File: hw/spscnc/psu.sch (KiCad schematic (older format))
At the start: 35 parts

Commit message: began routing of the i2so part
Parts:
- removed H17, H18, H21, H22, H23, H26, H28, H31: MountingHole_Pad, MountingHole:MountingHole_2.2mm_M2_Pad_Via, symbol Mechanical:MountingHole_Pad

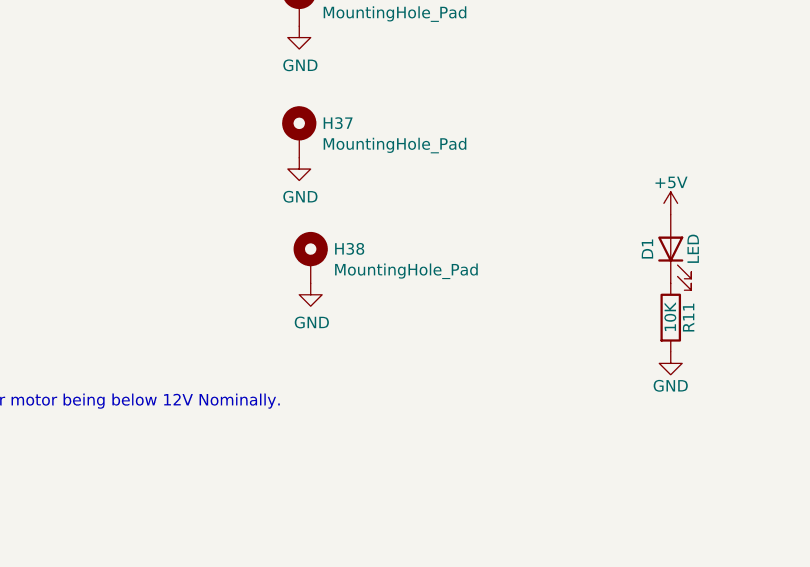
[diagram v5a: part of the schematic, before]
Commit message: Revision 1.1.0 With only critical corrections. Pending some work on the relays as that part could be remade from scratch for flexibility.
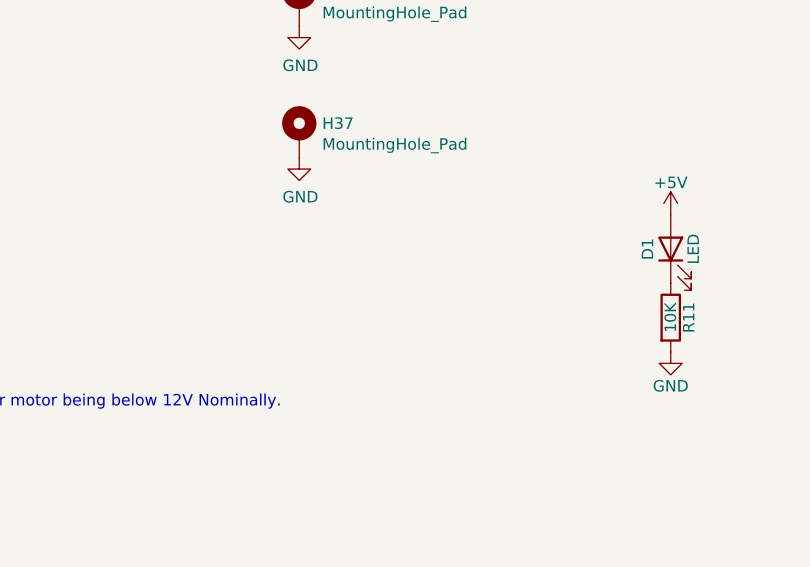
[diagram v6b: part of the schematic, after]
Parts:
- removed H38: MountingHole_Pad, MountingHole:MountingHole_2.2mm_M2_Pad_Via, symbol Mechanical:MountingHole_Pad
- H1, H11, H12, H13, H14, H15, H16, H19, H2, H20, H24, H25, H27, H29, H30, H32, H33, H34, H35, H36, H37: footprint MountingHole:MountingHole_2.2mm_M2_Pad_Via -> MountingHole:MountingHole_3.2mm_M3_Pad_Via
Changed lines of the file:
@@
 Sheet 2 17
 Title "Trinamic FluidNC CNC Controller"
-Date "2022-02-12"
-Rev "1.0.1"
+Date "2022-04-29"
+Rev "1.1.0"
 Comp ""
 Comment1 ""
@@
 F 0 "H1" H 6000 1474 50  0000 L CNN
 F 1 "MountingHole_Pad" H 6000 1383 50  0000 L CNN
-F 2 "MountingHole:MountingHole_2.2mm_M2_Pad_Via" H 5900 1425 50  0001 C CNN
+F 2 "MountingHole:MountingHole_3.2mm_M3_Pad_Via" H 5900 1425 50  0001 C CNN
 F 3 "~" H 5900 1425 50  0001 C CNN
 F 4 "DNP003" H 5900 1425 50  0001 C CNN "jlcpcb"
@@
 F 0 "H13" H 7250 1474 50  0000 L CNN
 F 1 "MountingHole_Pad" H 7250 1383 50  0000 L CNN
-F 2 "MountingHole:MountingHole_2.2mm_M2_Pad_Via" H 7150 1425 50  0001 C CNN
+F 2 "MountingHole:MountingHole_3.2mm_M3_Pad_Via" H 7150 1425 50  0001 C CNN
 F 3 "~" H 7150 1425 50  0001 C CNN
 F 4 "DNP003" H 7150 1425 50  0001 C CNN "jlcpcb"
@@
 F 0 "H12" H 6000 1999 50  0000 L CNN
 F 1 "MountingHole_Pad" H 6000 1908 50  0000 L CNN
-F 2 "MountingHole:MountingHole_2.2mm_M2_Pad_Via" H 5900 1950 50  0001 C CNN
+F 2 "MountingHole:MountingHole_3.2mm_M3_Pad_Via" H 5900 1950 50  0001 C CNN
 F 3 "~" H 5900 1950 50  0001 C CNN
 F 4 "DNP003" H 5900 1950 50  0001 C CNN "jlcpcb"
@@
 F 0 "H14" H 7250 2024 50  0000 L CNN
 F 1 "MountingHole_Pad" H 7250 1933 50  0000 L CNN
-F 2 "MountingHole:MountingHole_2.2mm_M2_Pad_Via" H 7150 1975 50  0001 C CNN
+F 2 "MountingHole:MountingHole_3.2mm_M3_Pad_Via" H 7150 1975 50  0001 C CNN
 F 3 "~" H 7150 1975 50  0001 C CNN
 F 4 "DNP003" H 7150 1975 50  0001 C CNN "jlcpcb"
@@
 F 0 "H2" H 5975 2574 50  0000 L CNN
 F 1 "MountingHole_Pad" H 5975 2483 50  0000 L CNN
-F 2 "MountingHole:MountingHole_2.2mm_M2_Pad_Via" H 5875 2525 50  0001 C CNN
+F 2 "MountingHole:MountingHole_3.2mm_M3_Pad_Via" H 5875 2525 50  0001 C CNN
 F 3 "~" H 5875 2525 50  0001 C CNN
 F 4 "DNP003" H 5875 2525 50  0001 C CNN "jlcpcb"
@@
 F 0 "H15" H 7275 2574 50  0000 L CNN
 F 1 "MountingHole_Pad" H 7275 2483 50  0000 L CNN
-F 2 "MountingHole:MountingHole_2.2mm_M2_Pad_Via" H 7175 2525 50  0001 C CNN
+F 2 "MountingHole:MountingHole_3.2mm_M3_Pad_Via" H 7175 2525 50  0001 C CNN
 F 3 "~" H 7175 2525 50  0001 C CNN
 F 4 "DNP003" H 7175 2525 50  0001 C CNN "jlcpcb"
@@
 F 0 "H19" H 8325 2599 50  0000 L CNN
 F 1 "MountingHole_Pad" H 8325 2508 50  0000 L CNN
-F 2 "MountingHole:MountingHole_2.2mm_M2_Pad_Via" H 8225 2550 50  0001 C CNN
+F 2 "MountingHole:MountingHole_3.2mm_M3_Pad_Via" H 8225 2550 50  0001 C CNN
 F 3 "~" H 8225 2550 50  0001 C CNN
 F 4 "DNP003" H 8225 2550 50  0001 C CNN "jlcpcb"
@@
 F 0 "H11" H 5975 3174 50  0000 L CNN
 F 1 "MountingHole_Pad" H 5975 3083 50  0000 L CNN
-F 2 "MountingHole:MountingHole_2.2mm_M2_Pad_Via" H 5875 3125 50  0001 C CNN
+F 2 "MountingHole:MountingHole_3.2mm_M3_Pad_Via" H 5875 3125 50  0001 C CNN
 F 3 "~" H 5875 3125 50  0001 C CNN
 F 4 "DNP003" H 5875 3125 50  0001 C CNN "jlcpcb"
@@
 F 0 "H16" H 7300 3149 50  0000 L CNN
 F 1 "MountingHole_Pad" H 7300 3058 50  0000 L CNN
-F 2 "MountingHole:MountingHole_2.2mm_M2_Pad_Via" H 7200 3100 50  0001 C CNN
+F 2 "MountingHole:MountingHole_3.2mm_M3_Pad_Via" H 7200 3100 50  0001 C CNN
 F 3 "~" H 7200 3100 50  0001 C CNN
 F 4 "DNP003" H 7200 3100 50  0001 C CNN "jlcpcb"
@@
 F 0 "H20" H 8375 3149 50  0000 L CNN
 F 1 "MountingHole_Pad" H 8375 3058 50  0000 L CNN
-F 2 "MountingHole:MountingHole_2.2mm_M2_Pad_Via" H 8275 3100 50  0001 C CNN
+F 2 "MountingHole:MountingHole_3.2mm_M3_Pad_Via" H 8275 3100 50  0001 C CNN
 F 3 "~" H 8275 3100 50  0001 C CNN
 F 4 "DNP003" H 8275 3100 50  0001 C CNN "jlcpcb"
@@
 F 0 "H24" H 9475 3149 50  0000 L CNN
 F 1 "MountingHole_Pad" H 9475 3058 50  0000 L CNN
-F 2 "MountingHole:MountingHole_2.2mm_M2_Pad_Via" H 9375 3100 50  0001 C CNN
+F 2 "MountingHole:MountingHole_3.2mm_M3_Pad_Via" H 9375 3100 50  0001 C CNN
 F 3 "~" H 9375 3100 50  0001 C CNN
 F 4 "DNP003" H 9375 3100 50  0001 C CNN "jlcpcb"
@@
 F 0 "H25" H 10375 1474 50  0000 L CNN
 F 1 "MountingHole_Pad" H 10375 1383 50  0000 L CNN
-F 2 "MountingHole:MountingHole_2.2mm_M2_Pad_Via" H 10275 1425 50  0001 C CNN
+F 2 "MountingHole:MountingHole_3.2mm_M3_Pad_Via" H 10275 1425 50  0001 C CNN
 F 3 "~" H 10275 1425 50  0001 C CNN
 F 4 "DNP003" H 10275 1425 50  0001 C CNN "jlcpcb"
@@
 F 0 "H27" H 10375 2599 50  0000 L CNN
 F 1 "MountingHole_Pad" H 10375 2508 50  0000 L CNN
-F 2 "MountingHole:MountingHole_2.2mm_M2_Pad_Via" H 10275 2550 50  0001 C CNN
+F 2 "MountingHole:MountingHole_3.2mm_M3_Pad_Via" H 10275 2550 50  0001 C CNN
 F 3 "~" H 10275 2550 50  0001 C CNN
 F 4 "DNP003" H 10275 2550 50  0001 C CNN "jlcpcb"
@@
 F 0 "H29" H 10275 3799 50  0000 L CNN
 F 1 "MountingHole_Pad" H 10275 3708 50  0000 L CNN
-F 2 "MountingHole:MountingHole_2.2mm_M2_Pad_Via" H 10175 3750 50  0001 C CNN
+F 2 "MountingHole:MountingHole_3.2mm_M3_Pad_Via" H 10175 3750 50  0001 C CNN
 F 3 "~" H 10175 3750 50  0001 C CNN
 F 4 "DNP003" H 10175 3750 50  0001 C CNN "jlcpcb"
@@
 F 0 "H30" H 10275 4349 50  0000 L CNN
 F 1 "MountingHole_Pad" H 10275 4258 50  0000 L CNN
-F 2 "MountingHole:MountingHole_2.2mm_M2_Pad_Via" H 10175 4300 50  0001 C CNN
+F 2 "MountingHole:MountingHole_3.2mm_M3_Pad_Via" H 10175 4300 50  0001 C CNN
 F 3 "~" H 10175 4300 50  0001 C CNN
 F 4 "DNP003" H 10175 4300 50  0001 C CNN "jlcpcb"
@@
 F 0 "H32" H 10325 5474 50  0000 L CNN
 F 1 "MountingHole_Pad" H 10325 5383 50  0000 L CNN
-F 2 "MountingHole:MountingHole_2.2mm_M2_Pad_Via" H 10225 5425 50  0001 C CNN
+F 2 "MountingHole:MountingHole_3.2mm_M3_Pad_Via" H 10225 5425 50  0001 C CNN
 F 3 "~" H 10225 5425 50  0001 C CNN
 F 4 "DNP003" H 10225 5425 50  0001 C CNN "jlcpcb"
@@
 F 0 "H33" H 9450 3849 50  0000 L CNN
 F 1 "MountingHole_Pad" H 9450 3758 50  0000 L CNN
-F 2 "MountingHole:MountingHole_2.2mm_M2_Pad_Via" H 9350 3800 50  0001 C CNN
+F 2 "MountingHole:MountingHole_3.2mm_M3_Pad_Via" H 9350 3800 50  0001 C CNN
 F 3 "~" H 9350 3800 50  0001 C CNN
 F 4 "DNP003" H 9350 3800 50  0001 C CNN "jlcpcb"
@@
 F 0 "H34" H 9500 4399 50  0000 L CNN
 F 1 "MountingHole_Pad" H 9500 4308 50  0000 L CNN
-F 2 "MountingHole:MountingHole_2.2mm_M2_Pad_Via" H 9400 4350 50  0001 C CNN
+F 2 "MountingHole:MountingHole_3.2mm_M3_Pad_Via" H 9400 4350 50  0001 C CNN
 F 3 "~" H 9400 4350 50  0001 C CNN
 F 4 "DNP003" H 9400 4350 50  0001 C CNN "jlcpcb"
@@
 F 0 "H35" H 7725 4174 50  0000 L CNN
 F 1 "MountingHole_Pad" H 7725 4083 50  0000 L CNN
-F 2 "MountingHole:MountingHole_2.2mm_M2_Pad_Via" H 7625 4125 50  0001 C CNN
+F 2 "MountingHole:MountingHole_3.2mm_M3_Pad_Via" H 7625 4125 50  0001 C CNN
 F 3 "~" H 7625 4125 50  0001 C CNN
 F 4 "DNP003" H 7625 4125 50  0001 C CNN "jlcpcb"
@@
 F 0 "H36" H 7725 4724 50  0000 L CNN
 F 1 "MountingHole_Pad" H 7725 4633 50  0000 L CNN
-F 2 "MountingHole:MountingHole_2.2mm_M2_Pad_Via" H 7625 4675 50  0001 C CNN
+F 2 "MountingHole:MountingHole_3.2mm_M3_Pad_Via" H 7625 4675 50  0001 C CNN
 F 3 "~" H 7625 4675 50  0001 C CNN
 F 4 "DNP003" H 7625 4675 50  0001 C CNN "jlcpcb"
@@
 F 0 "H37" H 7725 5299 50  0000 L CNN
 F 1 "MountingHole_Pad" H 7725 5208 50  0000 L CNN
-F 2 "MountingHole:MountingHole_2.2mm_M2_Pad_Via" H 7625 5250 50  0001 C CNN
+F 2 "MountingHole:MountingHole_3.2mm_M3_Pad_Via" H 7625 5250 50  0001 C CNN
 F 3 "~" H 7625 5250 50  0001 C CNN
 F 4 "DNP003" H 7625 5250 50  0001 C CNN "jlcpcb"
@@
 	1    0    0    -1
 $EndComp
-$Comp
-L Mechanical:MountingHole_Pad H?
-U 1 1 62012731
-P 7675 5800
-AR Path="/61E601B6/62012731" Ref="H?"  Part="1"
-AR Path="/6203D74D/62012731" Ref="H?"  Part="1"
-AR Path="/6203DA5D/62012731" Ref="H?"  Part="1"
-AR Path="/6203DFCF/62012731" Ref="H?"  Part="1"
-AR Path="/61C743E7/62012731" Ref="H38"  Part="1"
-F 0 "H38" H 7775 5849 50  0000 L CNN
-F 1 "MountingHole_Pad" H 7775 5758 50  0000 L CNN
-F 2 "MountingHole:MountingHole_2.2mm_M2_Pad_Via" H 7675 5800 50  0001 C CNN
-F 3 "~" H 7675 5800 50  0001 C CNN
-F 4 "DNP003" H 7675 5800 50  0001 C CNN "jlcpcb"
-	1    7675 5800
-	1    0    0    -1
-$EndComp
-$Comp
-L power:GND-power #PWR?
-U 1 1 6201273B
-P 7675 5900
-AR Path="/61E601B6/6201273B" Ref="#PWR?"  Part="1"
-AR Path="/6203D74D/6201273B" Ref="#PWR?"  Part="1"
-AR Path="/6203DA5D/6201273B" Ref="#PWR?"  Part="1"
-AR Path="/6203DFCF/6201273B" Ref="#PWR?"  Part="1"
-AR Path="/61C743E7/6201273B" Ref="#PWR0207"  Part="1"
-AR Path="/6201273B" Ref="#PWR0207"  Part="1"
-F 0 "#PWR0207" H 7675 5650 50  0001 C CNN
-F 1 "GND" H 7680 5727 50  0000 C CNN
-F 2 "" H 7675 5900 50  0001 C CNN
-F 3 "" H 7675 5900 50  0001 C CNN
-	1    7675 5900
-	1    0    0    -1
-$EndComp
